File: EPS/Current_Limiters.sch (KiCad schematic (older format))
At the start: 30 parts

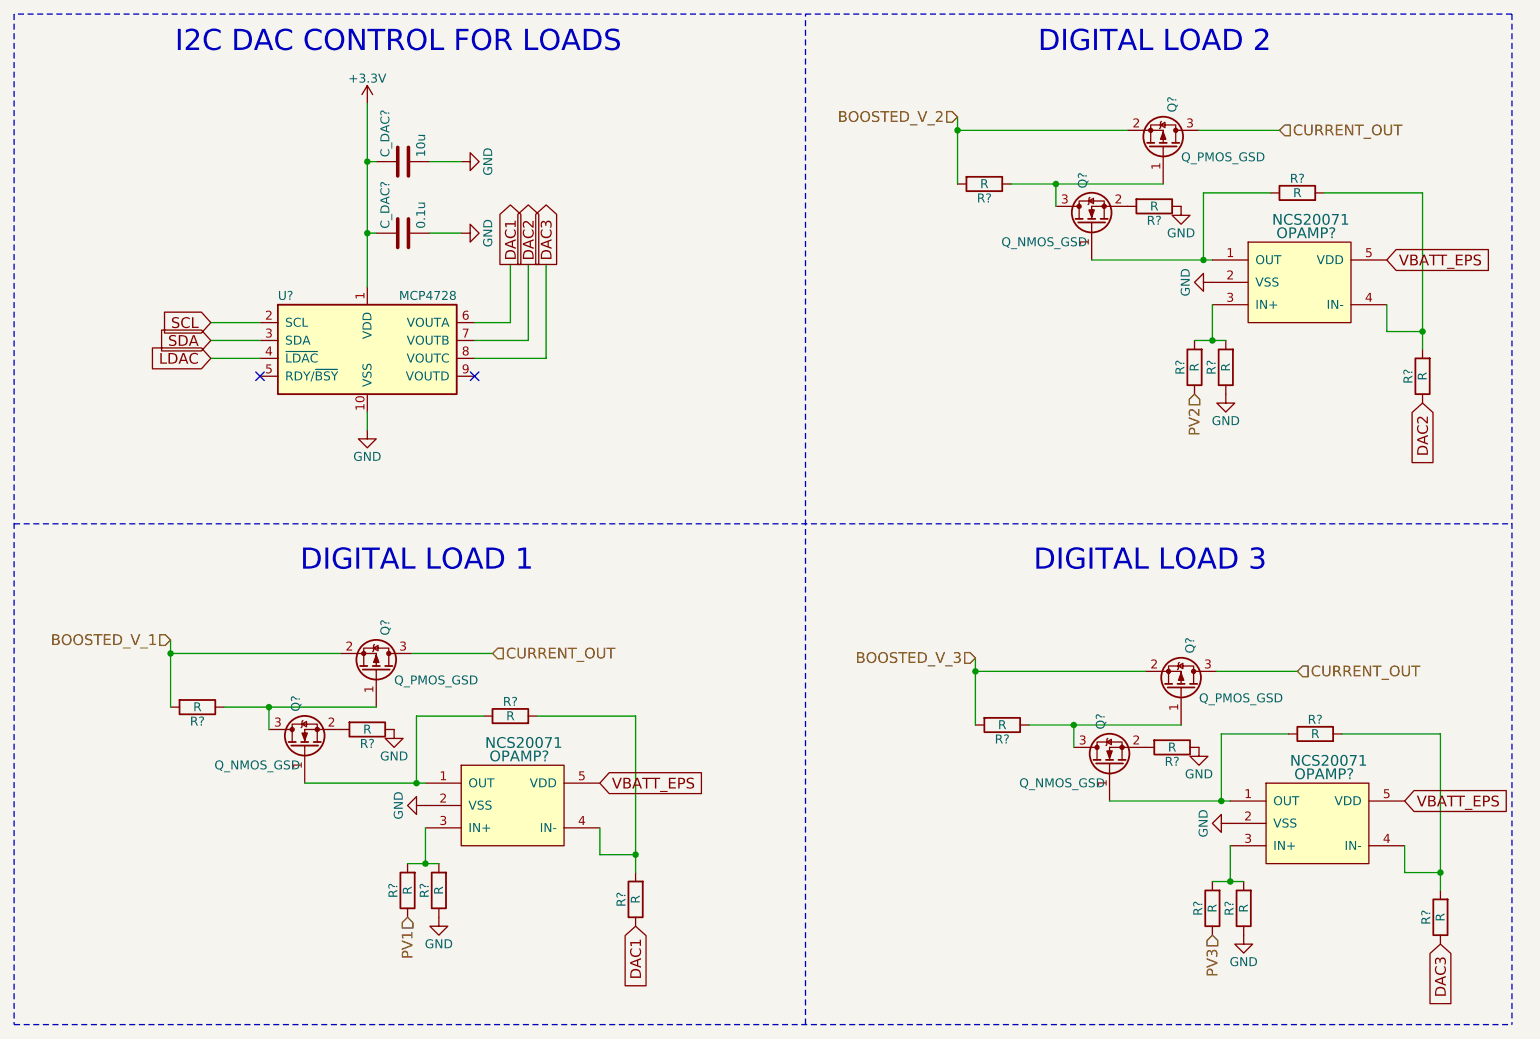
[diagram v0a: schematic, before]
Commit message: Finalized SCH (beta version) and started pcb
Capacitor banks might need to be reassigned to other locations.
No RBF pin on this SCH or PCB.
Battery gound deployment switch is fully mechanical (no mosfet switch on low side).
PCB of the prototype started. Main power converters and current measuring devices layed out.
SCH still requires ESD protection diodes!
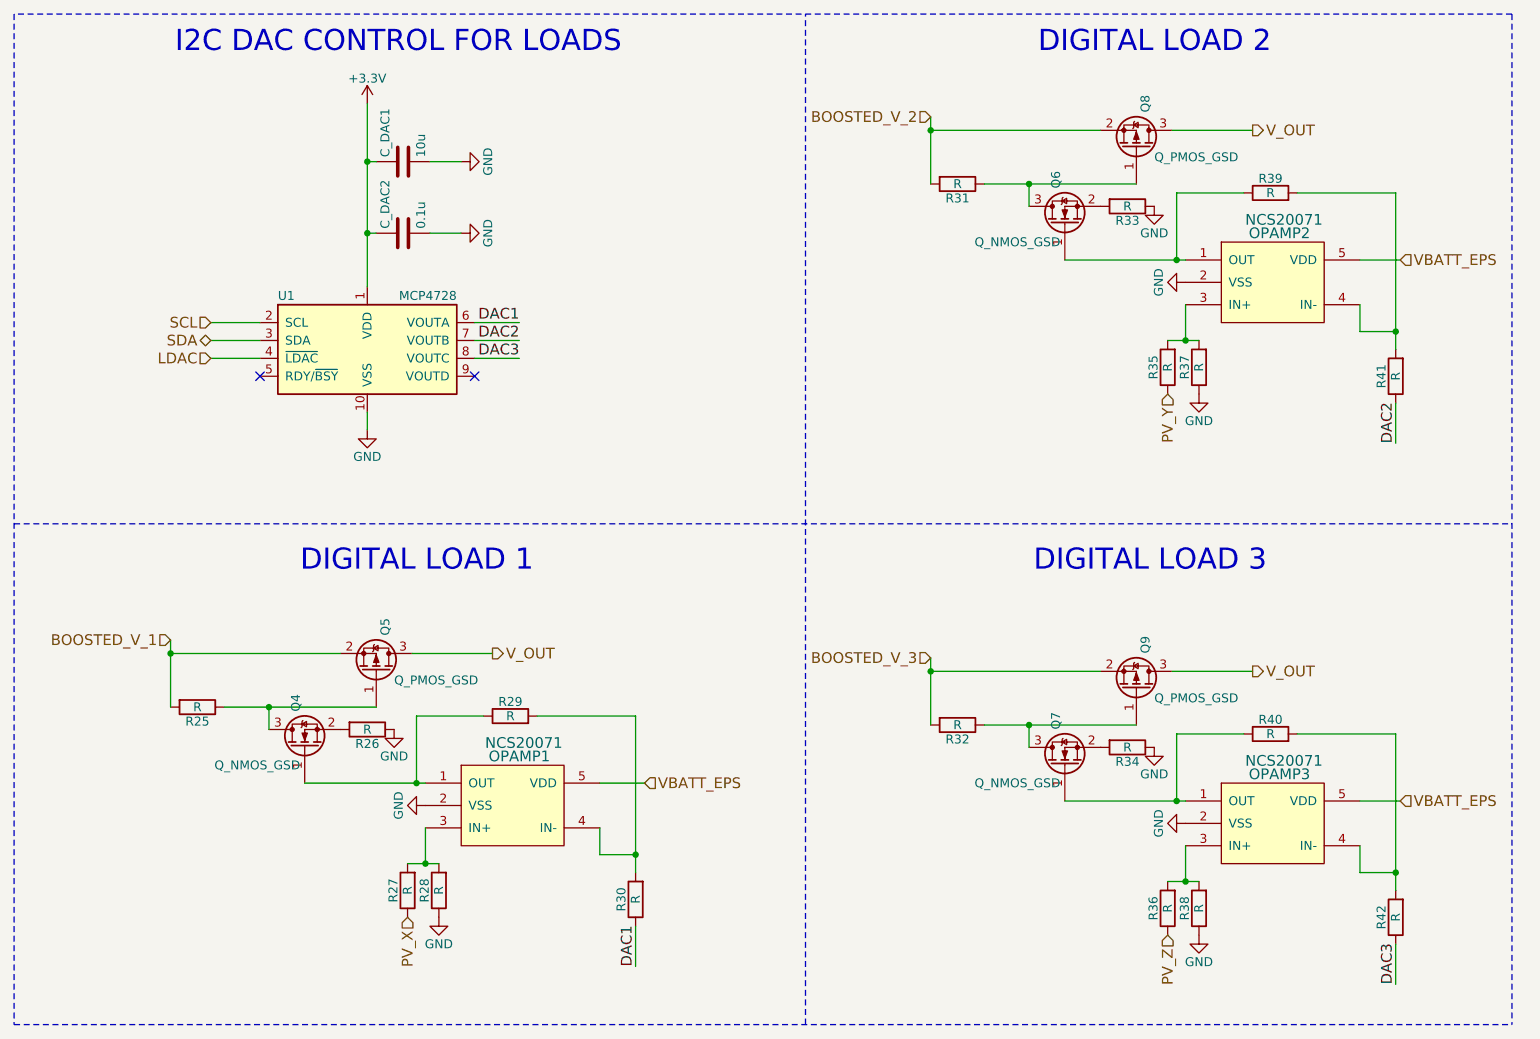
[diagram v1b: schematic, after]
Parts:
- C_DAC1: renamed from C_DAC?; footprint (none) -> Capacitors_SMD:C_0805
- C_DAC2: renamed from C_DAC?; footprint (none) -> Capacitors_SMD:C_0603
- OPAMP1, OPAMP2, OPAMP3: renamed from OPAMP?; footprint (none) -> TO_SOT_Packages_SMD:SOT-553
- Q4, Q5, Q6, Q7, Q8, Q9: renamed from Q?; footprint (none) -> TO_SOT_Packages_SMD:SOT-23
- R25, R26, R27, R28, R29, R30, R31, R32, R33, R34, R35, R36, R37, R38, R39, R40, R41, R42: renamed from R?; footprint (none) -> Resistors_SMD:R_0603
- gave numbers to parts that had none: 1
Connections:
- net CURRENT_OUT renamed V_OUT
- net PV1 renamed PV_X
- net PV2 renamed PV_Y
- net PV3 renamed PV_Z
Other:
- moved on the sheet: OPAMP2, OPAMP3, Q6, Q7, Q8, Q9, R31, R32, R33, R34, R35, R36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

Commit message: PCB updated
Added testpoints and updated PCB
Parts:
- added TP16, TP17, TP18, TP19, TP20, TP21, TP22, TP23, TP24: TEST, Measurement_Points:Measurement_Point_Round-SMD-Pad_Small, symbol TEST
- Q5, Q8, Q9: value Q_PMOS_GSD -> PMOS_DIGITAL_LOAD?
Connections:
- net DAC1: now also TP18.1
- net DAC2: now also TP19.1
- net DAC3: now also TP20.1
- net at OPAMP2.1 (OUT), Q6.1 (G), R39.1: now also TP24.1
- net at Q6.3 (D), Q8.1 (G), R31.1: now also TP23.1
- net at OPAMP3.1 (OUT), Q7.1 (G), R40.1: now also TP22.1
- net at Q7.3 (D), Q9.1 (G), R32.1: now also TP21.1
- net at OPAMP1.1 (OUT), Q4.1 (G), R29.1: now also TP17.1
- net at Q4.3 (D), Q5.1 (G), R25.1: now also TP16.1
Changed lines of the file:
@@
 $EndComp
 $Comp
-L GND #PWR097
+L GND #PWR096
 U 1 1 5A8CBE86
 P 8525 2275
-F 0 "#PWR097" H 8525 2025 50  0001 C CNN
+F 0 "#PWR096" H 8525 2025 50  0001 C CNN
 F 1 "GND" H 8525 2125 50  0000 C CNN
 F 2 "" H 8525 2275 50  0001 C CNN
@@
 $EndComp
 $Comp
-L GND #PWR098
+L GND #PWR097
 U 1 1 5A8CBF8A
 P 8600 2900
-F 0 "#PWR098" H 8600 2650 50  0001 C CNN
+F 0 "#PWR097" H 8600 2650 50  0001 C CNN
 F 1 "GND" H 8600 2750 50  0000 C CNN
 F 2 "" H 8600 2900 50  0001 C CNN
@@
 P 8250 1525
 F 0 "Q8" H 8450 1575 50  0000 L CNN
-F 1 "Q_PMOS_GSD" V 8200 1625 50  0000 L CNN
+F 1 "PMOS_DIGITAL_LOAD?" V 8200 1625 50  0000 L CNN
 F 2 "TO_SOT_Packages_SMD:SOT-23" H 8450 1625 50  0001 C CNN
 F 3 "" H 8250 1525 50  0001 C CNN
@@
 $EndComp
 $Comp
-L GND #PWR099
+L GND #PWR098
 U 1 1 5A8CC6C2
 P 8350 1850
-F 0 "#PWR099" H 8350 1600 50  0001 C CNN
+F 0 "#PWR098" H 8350 1600 50  0001 C CNN
 F 1 "GND" H 8350 1700 50  0000 C CNN
 F 2 "" H 8350 1850 50  0001 C CNN
@@
 NoConn ~ 4550 2800
 $Comp
-L GND #PWR0100
+L GND #PWR099
 U 1 1 5A8E6877
 P 3950 3100
-F 0 "#PWR0100" H 3950 2850 50  0001 C CNN
+F 0 "#PWR099" H 3950 2850 50  0001 C CNN
 F 1 "GND" H 3950 2950 50  0000 C CNN
 F 2 "" H 3950 3100 50  0001 C CNN
@@
 $EndComp
 $Comp
-L +3.3V #PWR0101
+L +3.3V #PWR0100
 U 1 1 5A8E687E
 P 3950 1275
-F 0 "#PWR0101" H 3950 1125 50  0001 C CNN
+F 0 "#PWR0100" H 3950 1125 50  0001 C CNN
 F 1 "+3.3V" H 3950 1415 50  0000 C CNN
 F 2 "" H 3950 1275 50  0001 C CNN
@@
 $EndComp
 $Comp
-L GND #PWR0102
+L GND #PWR0101
 U 1 1 5A8E6892
 P 4475 2000
-F 0 "#PWR0102" H 4475 1750 50  0001 C CNN
+F 0 "#PWR0101" H 4475 1750 50  0001 C CNN
 F 1 "GND" H 4475 1850 50  0000 C CNN
 F 2 "" H 4475 2000 50  0001 C CNN
@@
 $EndComp
 $Comp
-L GND #PWR0103
+L GND #PWR0102
 U 1 1 5A8E6898
 P 4475 1600
-F 0 "#PWR0103" H 4475 1350 50  0001 C CNN
+F 0 "#PWR0102" H 4475 1350 50  0001 C CNN
 F 1 "GND" H 4475 1450 50  0000 C CNN
 F 2 "" H 4475 1600 50  0001 C CNN
@@
 $EndComp
 $Comp
-L GND #PWR0104
+L GND #PWR0103
 U 1 1 5A8E6C4C
 P 8525 5300
-F 0 "#PWR0104" H 8525 5050 50  0001 C CNN
+F 0 "#PWR0103" H 8525 5050 50  0001 C CNN
 F 1 "GND" H 8525 5150 50  0000 C CNN
 F 2 "" H 8525 5300 50  0001 C CNN
@@
 $EndComp
 $Comp
-L GND #PWR0105
+L GND #PWR0104
 U 1 1 5A8E6C5A
 P 8600 5925
-F 0 "#PWR0105" H 8600 5675 50  0001 C CNN
+F 0 "#PWR0104" H 8600 5675 50  0001 C CNN
 F 1 "GND" H 8600 5775 50  0000 C CNN
 F 2 "" H 8600 5925 50  0001 C CNN
@@
 P 8250 4550
 F 0 "Q9" H 8450 4600 50  0000 L CNN
-F 1 "Q_PMOS_GSD" V 8200 4650 50  0000 L CNN
+F 1 "PMOS_DIGITAL_LOAD?" V 8200 4650 50  0000 L CNN
 F 2 "TO_SOT_Packages_SMD:SOT-23" H 8450 4650 50  0001 C CNN
 F 3 "" H 8250 4550 50  0001 C CNN
@@
 $EndComp
 $Comp
-L GND #PWR0106
+L GND #PWR0105
 U 1 1 5A8E6C87
 P 8350 4875
-F 0 "#PWR0106" H 8350 4625 50  0001 C CNN
+F 0 "#PWR0105" H 8350 4625 50  0001 C CNN
 F 1 "GND" H 8350 4725 50  0000 C CNN
 F 2 "" H 8350 4875 50  0001 C CNN
@@
 $EndComp
 $Comp
-L GND #PWR0107
+L GND #PWR0106
 U 1 1 5A8E6E7B
 P 4275 5200
-F 0 "#PWR0107" H 4275 4950 50  0001 C CNN
+F 0 "#PWR0106" H 4275 4950 50  0001 C CNN
 F 1 "GND" H 4275 5050 50  0000 C CNN
 F 2 "" H 4275 5200 50  0001 C CNN
@@
 $EndComp
 $Comp
-L GND #PWR0108
+L GND #PWR0107
 U 1 1 5A8E6E89
 P 4350 5825
-F 0 "#PWR0108" H 4350 5575 50  0001 C CNN
+F 0 "#PWR0107" H 4350 5575 50  0001 C CNN
 F 1 "GND" H 4350 5675 50  0000 C CNN
 F 2 "" H 4350 5825 50  0001 C CNN
@@
 P 4000 4450
 F 0 "Q5" H 4200 4500 50  0000 L CNN
-F 1 "Q_PMOS_GSD" V 3950 4550 50  0000 L CNN
+F 1 "PMOS_DIGITAL_LOAD?" V 3950 4550 50  0000 L CNN
 F 2 "TO_SOT_Packages_SMD:SOT-23" H 4200 4550 50  0001 C CNN
 F 3 "" H 4000 4450 50  0001 C CNN
@@
 $EndComp
 $Comp
-L GND #PWR0109
+L GND #PWR0108
 U 1 1 5A8E6EB6
 P 4100 4775
-F 0 "#PWR0109" H 4100 4525 50  0001 C CNN
+F 0 "#PWR0108" H 4100 4525 50  0001 C CNN
 F 1 "GND" H 4100 4625 50  0000 C CNN
 F 2 "" H 4100 4775 50  0001 C CNN
@@
 	4475 1600 4300 1600
 Wire Wire Line
-	4550 2500 4800 2500
+	4550 2500 5050 2500
 Wire Wire Line
 	8425 5625 8600 5625
@@
 	5500 5075 5250 5075
 Wire Wire Line
-	4550 2600 4800 2600
-Wire Wire Line
-	4800 2700 4550 2700
+	4550 2600 5200 2600
+Wire Wire Line
+	4550 2700 5325 2700
 Connection ~ 5450 5475
 Wire Wire Line
@@
 Wire Wire Line
 	9700 3175 9700 2950
+Wire Wire Line
+	5325 2700 5325 2675
+Wire Wire Line
+	5200 2600 5200 2575
+Wire Wire Line
+	5050 2500 5050 2475
+$Comp
+L TEST TP18
+U 1 1 5A9ED5A0
+P 5050 2475
+F 0 "TP18" H 5050 2775 50  0000 C BNN
+F 1 "TEST" H 5050 2725 50  0000 C CNN
+F 2 "Measurement_Points:Measurement_Point_Round-SMD-Pad_Small" H 5050 2475 50  0001 C CNN
+F 3 "" H 5050 2475 50  0001 C CNN
+	1    5050 2475
+	1    0    0    -1
+$EndComp
+$Comp
+L TEST TP19
+U 1 1 5A9ED62C
+P 5200 2575
+F 0 "TP19" H 5200 2875 50  0000 C BNN
+F 1 "TEST" H 5200 2825 50  0000 C CNN
+F 2 "Measurement_Points:Measurement_Point_Round-SMD-Pad_Small" H 5200 2575 50  0001 C CNN
+F 3 "" H 5200 2575 50  0001 C CNN
+	1    5200 2575
+	1    0    0    -1
+$EndComp
+$Comp
+L TEST TP20
+U 1 1 5A9ED6A2
+P 5325 2675
+F 0 "TP20" H 5325 2975 50  0000 C BNN
+F 1 "TEST" H 5325 2925 50  0000 C CNN
+F 2 "Measurement_Points:Measurement_Point_Round-SMD-Pad_Small" H 5325 2675 50  0001 C CNN
+F 3 "" H 5325 2675 50  0001 C CNN
+	1    5325 2675
+	1    0    0    -1
+$EndComp
+$Comp
+L TEST TP23
+U 1 1 5A9EDBF8
+P 6925 1950
+F 0 "TP23" H 6925 2250 50  0000 C BNN
+F 1 "TEST" H 6925 2200 50  0000 C CNN
+F 2 "Measurement_Points:Measurement_Point_Round-SMD-Pad_Small" H 6925 1950 50  0001 C CNN
+F 3 "" H 6925 1950 50  0001 C CNN
+	1    6925 1950
+	1    0    0    -1
+$EndComp
+Wire Wire Line
+	7500 1725 7500 1950
+Connection ~ 7500 1725
+Wire Wire Line
+	7500 1950 6925 1950
+Wire Wire Line
+	7950 2150 7950 2250
+Wire Wire Line
+	7950 2250 6925 2250
+Connection ~ 7950 2150
+$Comp
+L TEST TP24
+U 1 1 5A9EE049
+P 6925 2250
+F 0 "TP24" H 6925 2550 50  0000 C BNN
+F 1 "TEST" H 6925 2500 50  0000 C CNN
+F 2 "Measurement_Points:Measurement_Point_Round-SMD-Pad_Small" H 6925 2250 50  0001 C CNN
+F 3 "" H 6925 2250 50  0001 C CNN
+	1    6925 2250
+	1    0    0    -1
+$EndComp
+$Comp
+L TEST TP21
+U 1 1 5A9EE0D2
+P 6900 4925
+F 0 "TP21" H 6900 5225 50  0000 C BNN
+F 1 "TEST" H 6900 5175 50  0000 C CNN
+F 2 "Measurement_Points:Measurement_Point_Round-SMD-Pad_Small" H 6900 4925 50  0001 C CNN
+F 3 "" H 6900 4925 50  0001 C CNN
+	1    6900 4925
+	1    0    0    -1
+$EndComp
+$Comp
+L TEST TP22
+U 1 1 5A9EE250
+P 6900 5325
+F 0 "TP22" H 6900 5625 50  0000 C BNN
+F 1 "TEST" H 6900 5575 50  0000 C CNN
+F 2 "Measurement_Points:Measurement_Point_Round-SMD-Pad_Small" H 6900 5325 50  0001 C CNN
+F 3 "" H 6900 5325 50  0001 C CNN
+	1    6900 5325
+	1    0    0    -1
+$EndComp
+Wire Wire Line
+	6900 4925 7500 4925
+Wire Wire Line
+	7500 4925 7500 4750
+Connection ~ 7500 4750
+Wire Wire Line
+	6900 5325 7950 5325
+Wire Wire Line
+	7950 5325 7950 5175
+Connection ~ 7950 5175
+$Comp
+L TEST TP16
+U 1 1 5A9EE5C6
+P 2550 4900
+F 0 "TP16" H 2550 5200 50  0000 C BNN
+F 1 "TEST" H 2550 5150 50  0000 C CNN
+F 2 "Measurement_Points:Measurement_Point_Round-SMD-Pad_Small" H 2550 4900 50  0001 C CNN
+F 3 "" H 2550 4900 50  0001 C CNN
+	1    2550 4900
+	1    0    0    -1
+$EndComp
+$Comp
+L TEST TP17
+U 1 1 5A9EE750
+P 2550 5325
+F 0 "TP17" H 2550 5625 50  0000 C BNN
+F 1 "TEST" H 2550 5575 50  0000 C CNN
+F 2 "Measurement_Points:Measurement_Point_Round-SMD-Pad_Small" H 2550 5325 50  0001 C CNN
+F 3 "" H 2550 5325 50  0001 C CNN
+	1    2550 5325
+	1    0    0    -1
+$EndComp
+Wire Wire Line
+	2550 4900 3225 4900
+Wire Wire Line
+	3225 4900 3225 4650
+Connection ~ 3225 4650
+Wire Wire Line
+	2550 5325 3700 5325
+Wire Wire Line
+	3700 5325 3700 5075
+Connection ~ 3700 5075
 $EndSCHEMATC
